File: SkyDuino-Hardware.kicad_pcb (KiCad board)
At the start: 4 copper layers, 123 x 56 mm, 83 parts, among them J1 24V, J11 DBG, J12 USB-A RMT, J13 DISP, J14 USB_C Artisan, J2 BT, J4 Drum, J5 Exhaust, J6 Cooling, J7 Cooling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

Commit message: JLCPCB and Revision tagging
- Generate JLCPCB assembly files: BoM & Position
- Tag revisions based on Git Tags
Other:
- board text added: "${TITLE} ${GIT_TAG} ${COMMIT_HASH}"
- board text removed: "${TITLE} Rev: ${RELEASE_VERSION} ${COMMIT_HASH} ${GIT_TAG}"
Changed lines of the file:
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@@
 	(title_block
 		(title "Skyduino Roaster")
-		(date "2024-05-13")
-		(rev "${RELEASE_VERSION}")
+		(date "${COMMIT_DATE}")
+		(rev "${REVISION}")
 		(company "Raz-1")
 		(comment 2 "${COMMIT_DATE_LONG}")
@@
 	(property "COMMIT_HASH" "beefbeef")
 	(property "GIT_TAG" "")
-	(property "RELEASE_VERSION" "0.5.dev")
+	(property "REVISION" "")
 	(net 0 "")
 	(net 1 "Net-(ACL1-Pin_1)")
@@
 		)
 	)
-	(gr_text "${TITLE} Rev: ${RELEASE_VERSION}\n${COMMIT_HASH} ${GIT_TAG}"
+	(gr_text "${TITLE} ${GIT_TAG}\n${COMMIT_HASH}"
 		(at 150 86 0)
 		(layer "B.SilkS")

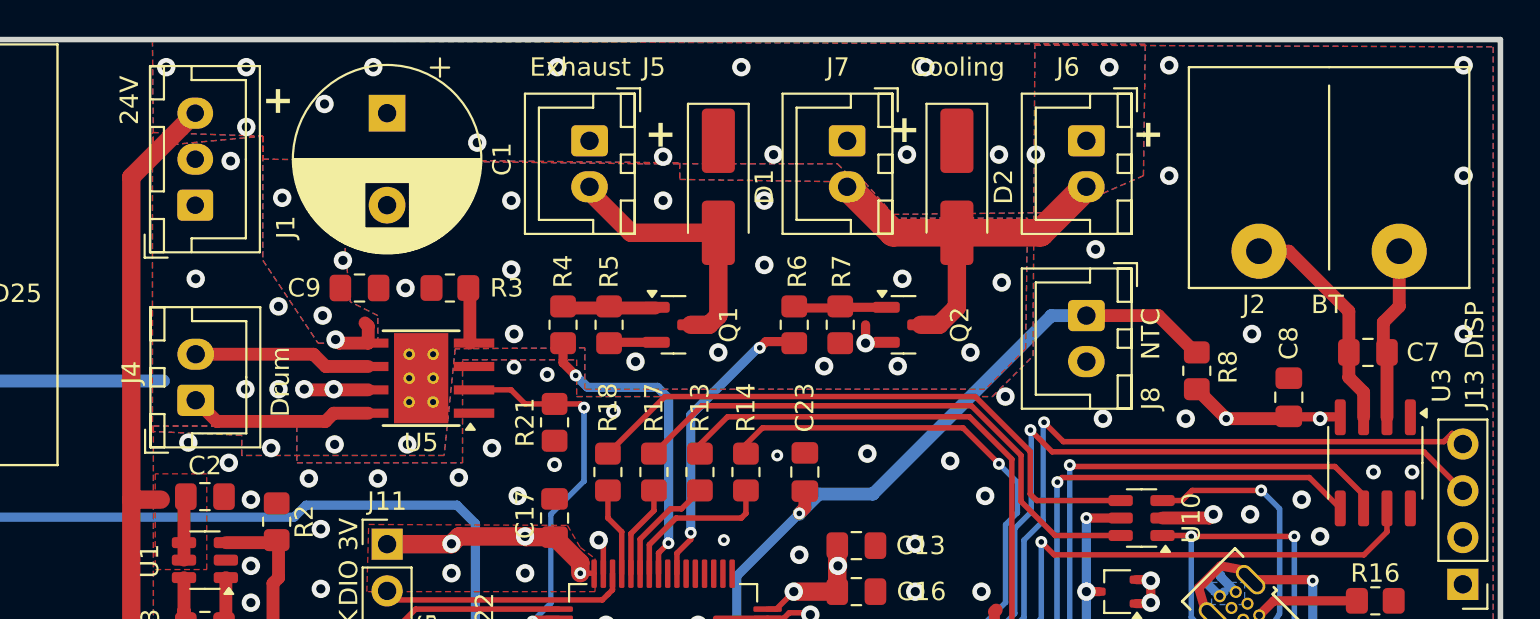
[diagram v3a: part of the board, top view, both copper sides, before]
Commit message: Make it fit the vented coffin enclosure.
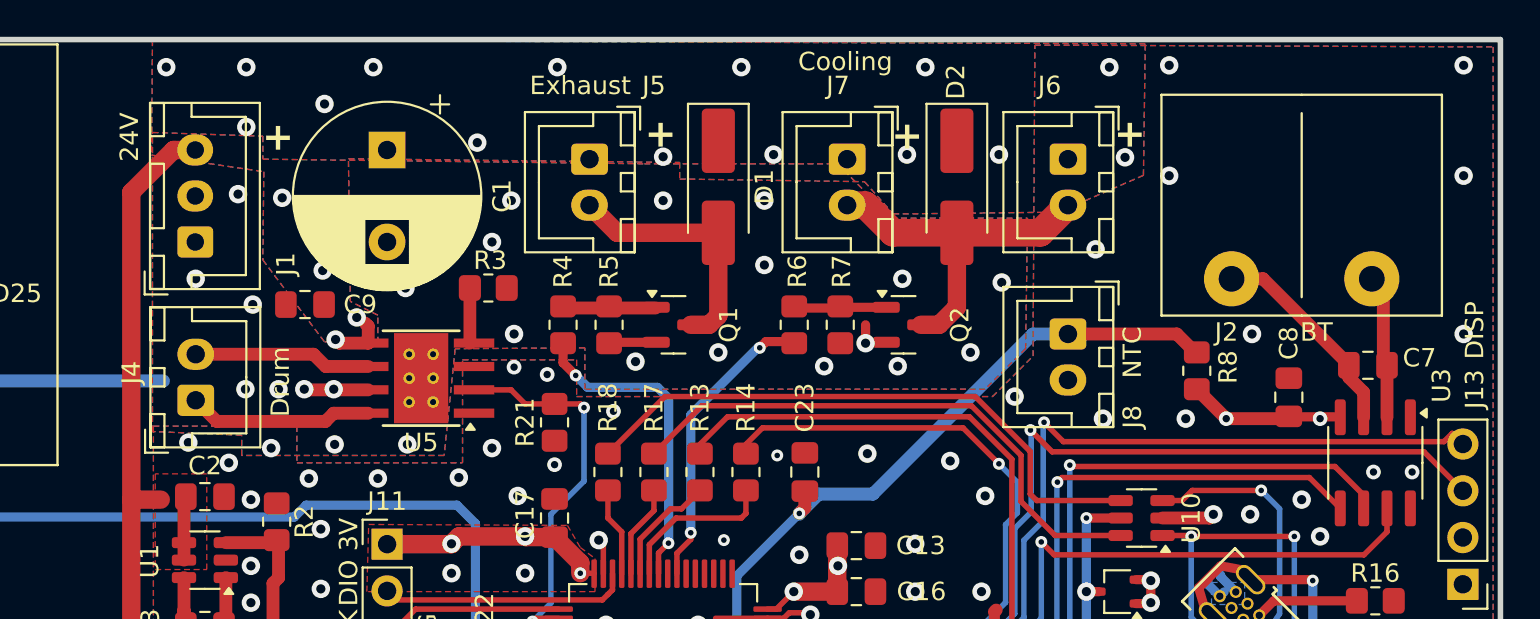
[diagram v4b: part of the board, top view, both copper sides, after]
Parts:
- moved C9 3.10 mm to (164.0, 94.4), turned to 180 degrees
- moved J2 2.11 mm to (218.2, 89.0)
- moved R3 2.09 mm to (174.0, 93.5), turned to 0 degrees
- moved C1 2.00 mm to (168.5, 86.0)
- moved J1 2.00 mm to (158.1, 91.0)
- moved J6 1.41 mm to (205.5, 86.5)
- moved J8 1.41 mm to (205.5, 96.0)
- moved J5 1.00 mm to (179.5, 86.5)
- moved J7 1.00 mm to (193.5, 86.5)
- moved C7 0.70 mm to (221.8, 97.7)
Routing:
- net Net-(J2-Pin_2): track 9.38 -> 7.09 mm
- net COOL: track 21.6 -> 19.8 mm
- net NTC: track 39.6 -> 37.8 mm
- net +24V: track 64.0 -> 62.7 mm
- net Net-(J2-Pin_1): track 12.3 -> 11.5 mm
- net EXHT: track 14.4 -> 13.8 mm

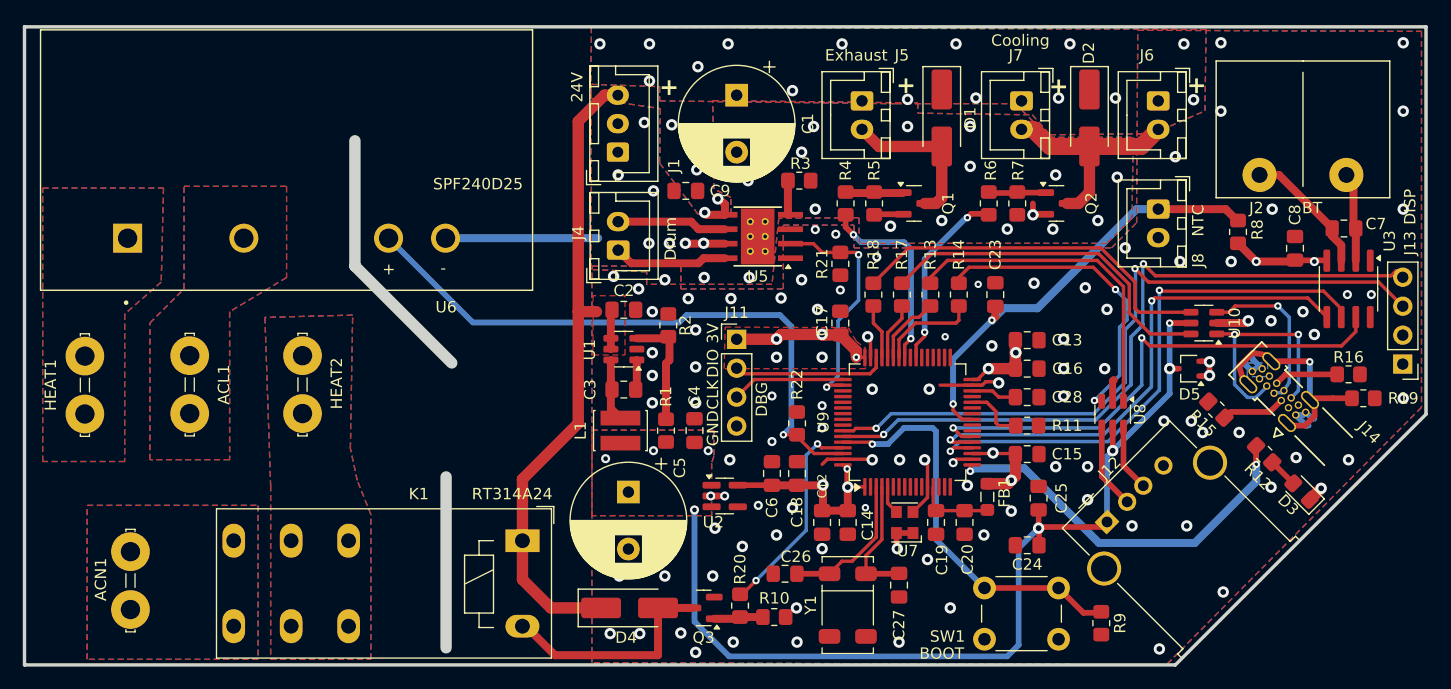
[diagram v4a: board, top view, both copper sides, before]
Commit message: Reposition SSR to fit into vented enclosure
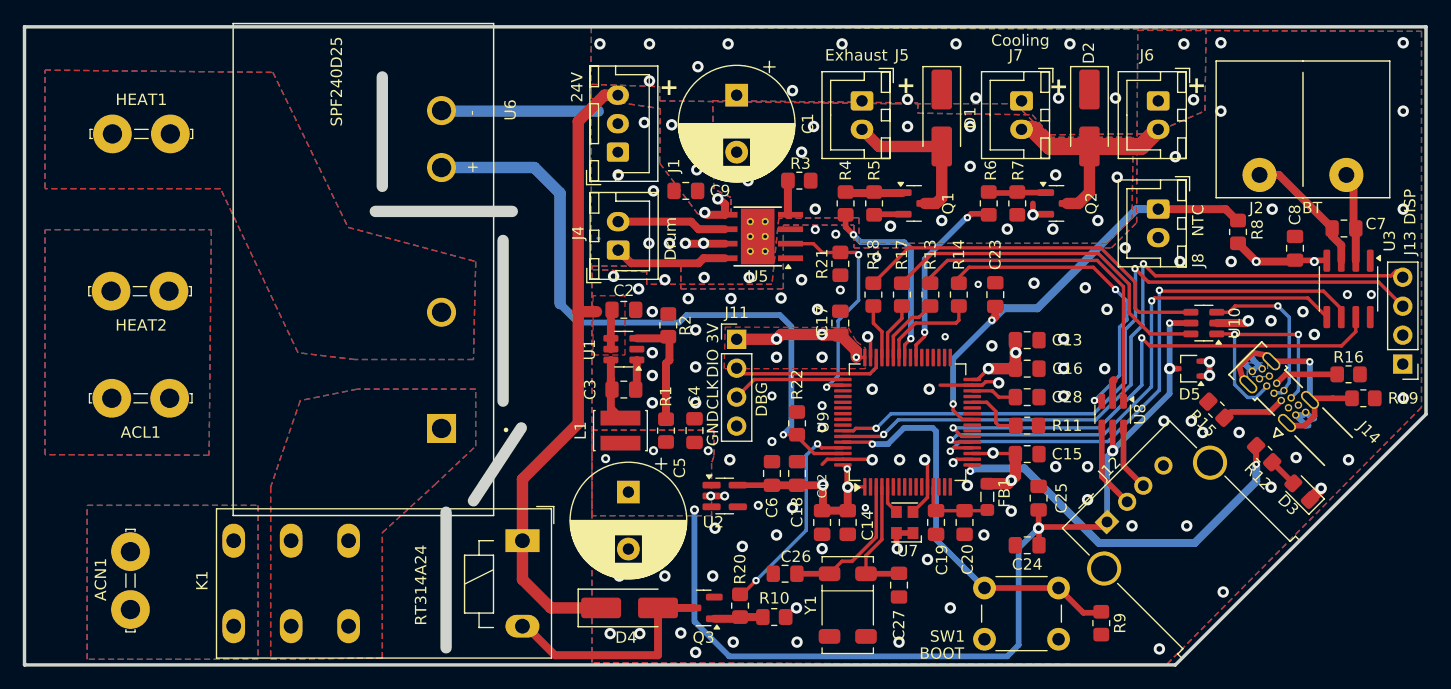
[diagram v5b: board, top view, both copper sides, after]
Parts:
- moved HEAT1 22.6 mm to (116.3, 89.4), turned to 0 degrees
- moved HEAT2 16.4 mm to (116.1, 103.2), turned to 0 degrees
- moved U6 13.9 mm to (142.6, 101.3), turned to 90 degrees
- moved ACL1 4.46 mm to (116.2, 112.6), turned to 0 degrees
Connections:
- HEAT2 pad 1: Net-(HEAT2-Pin_1) -> Net-(ACL1-Pin_1)
- K1 pad 11: Net-(HEAT2-Pin_1) -> Net-(K1-Pad11)
- K1 pad 12: Net-(HEAT2-Pin_1) -> Net-(K1-Pad11)
- U6 pad 1: Net-(HEAT1-Pin_1) -> Net-(K1-Pad11)
- U6 pad 2: Net-(ACL1-Pin_1) -> Net-(HEAT1-Pin_1)
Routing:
- net SSR: track 54.8 -> 58.4 mm
- added copper zone on B.Cu, net Net-(K1-Pad11)
- added copper zone on F.Cu, net Net-(K1-Pad11)
- added copper zone on In1.Cu, net Net-(K1-Pad11)
- added copper zone on In2.Cu, net Net-(K1-Pad11)
- removed copper zone on B.Cu, net Net-(HEAT2-Pin_1)
- removed copper zone on F.Cu, net Net-(HEAT2-Pin_1)
- removed copper zone on In1.Cu, net Net-(HEAT2-Pin_1)
- removed copper zone on In2.Cu, net Net-(HEAT2-Pin_1)
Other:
- outline, holes or cut-outs redrawn

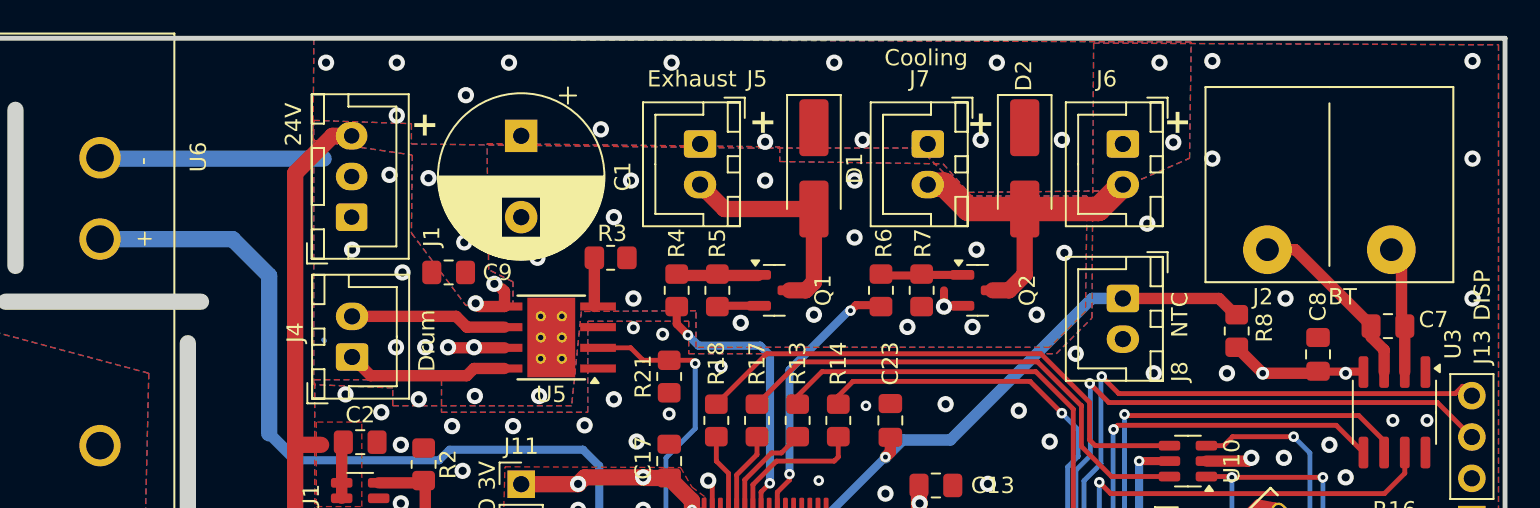
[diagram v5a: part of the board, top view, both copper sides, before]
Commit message: Move capacitor, 24v conn & TC conn
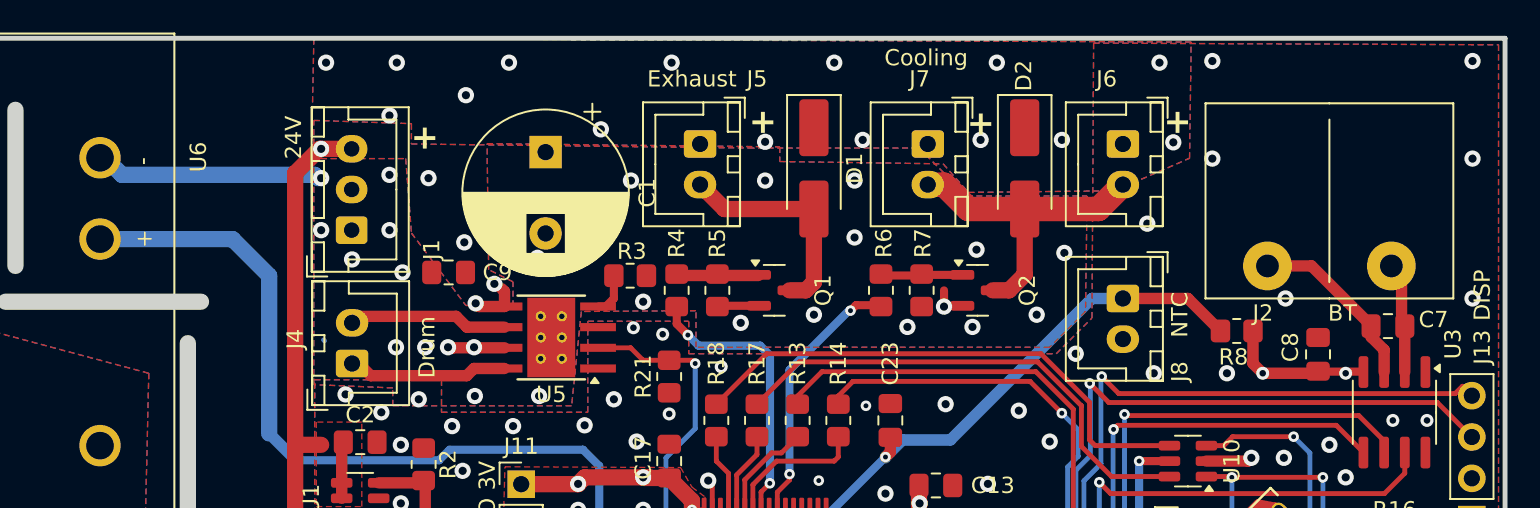
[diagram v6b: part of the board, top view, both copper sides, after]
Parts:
- moved C1 1.80 mm to (170.0, 87.0)
- moved R3 1.63 mm to (175.2, 94.6)
- moved J2 1.00 mm to (218.2, 90.0)
- moved J1 0.80 mm to (158.1, 91.8)
- moved J4 0.40 mm to (158.1, 100.0)
- turned R8 to 180 degrees
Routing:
- net Net-(U5-ILIM): track 3.23 -> 2.58 mm
- net NTC: track 37.8 -> 37.2 mm
- net +3V3: track 57.3 -> 57.9 mm
- net Net-(J2-Pin_1): track 11.5 -> 12.1 mm
- net +24V: track 62.7 -> 62.4 mm, vias 19 -> 20
- net GND: track 53.0 -> 53.1 mm, vias 125 -> 128

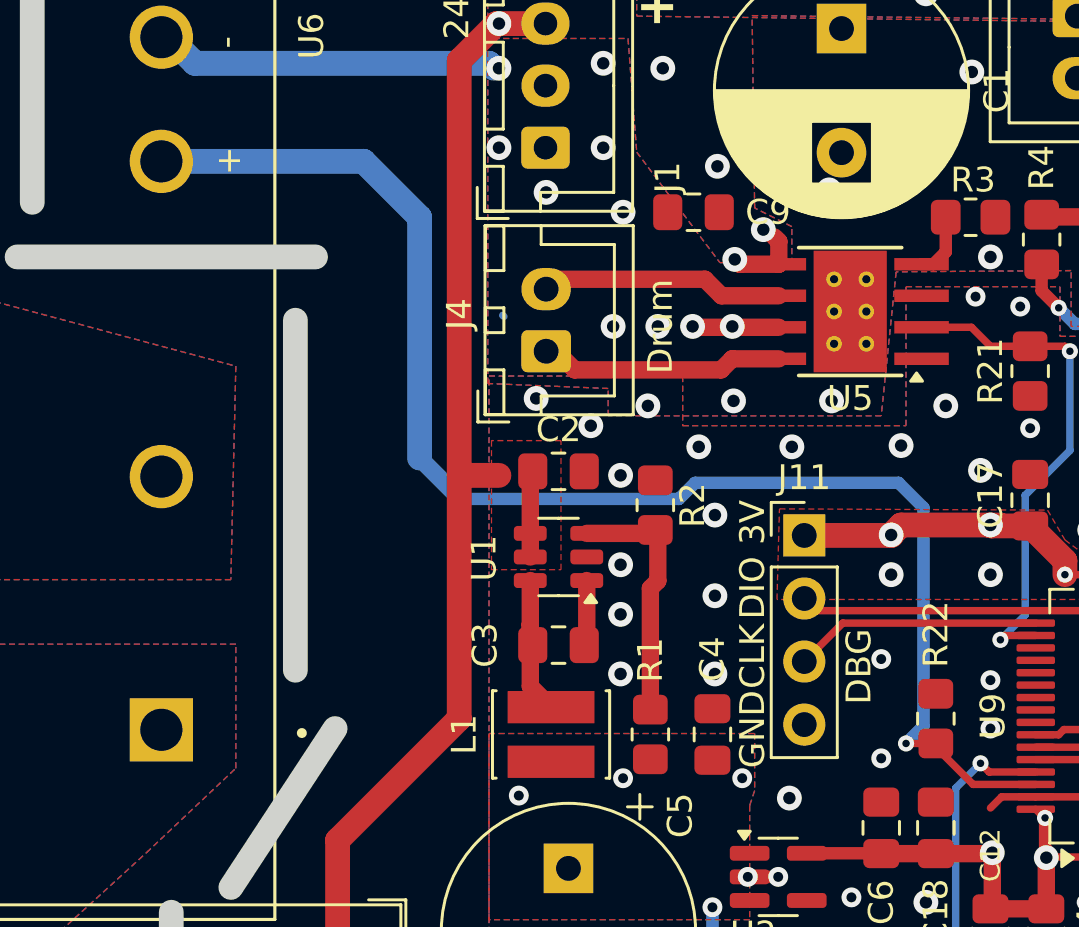
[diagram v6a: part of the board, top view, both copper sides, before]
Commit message: Reroute SSR control track
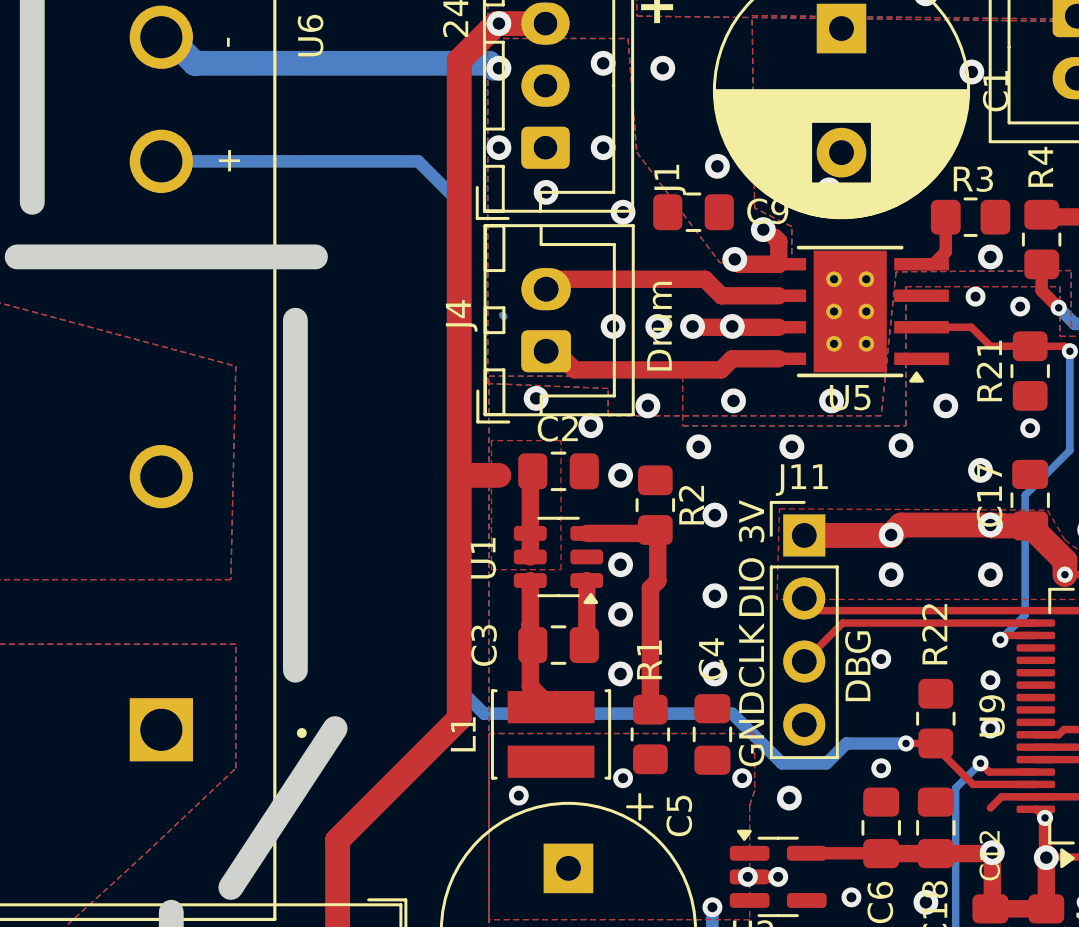
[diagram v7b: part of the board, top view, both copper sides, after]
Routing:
- net SSR: track 58.4 -> 57.8 mm

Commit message: Fix DRC
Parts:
- moved C7 0.50 mm to (221.8, 98.2)
- moved J4 0.50 mm to (158.1, 100.5)
- moved R8 0.10 mm to (212.5, 98.1)
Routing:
- net GND: track 53.1 -> 54.6 mm, vias 128 -> 127
- net +24V: track 62.4 -> 61.1 mm
- net Net-(J2-Pin_2): track 7.09 -> 7.87 mm
- net SSR: track 57.8 -> 57.2 mm
